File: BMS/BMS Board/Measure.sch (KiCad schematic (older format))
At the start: 53 parts, among them U1 INA149AID, U10 INA149AID, U11 INA149AID, U12 INA149AID, U13 INA149AID, U14 INA149AID, U15 INA149AID, U16 INA149AID, U17 INA149AID, U18 INA149AID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

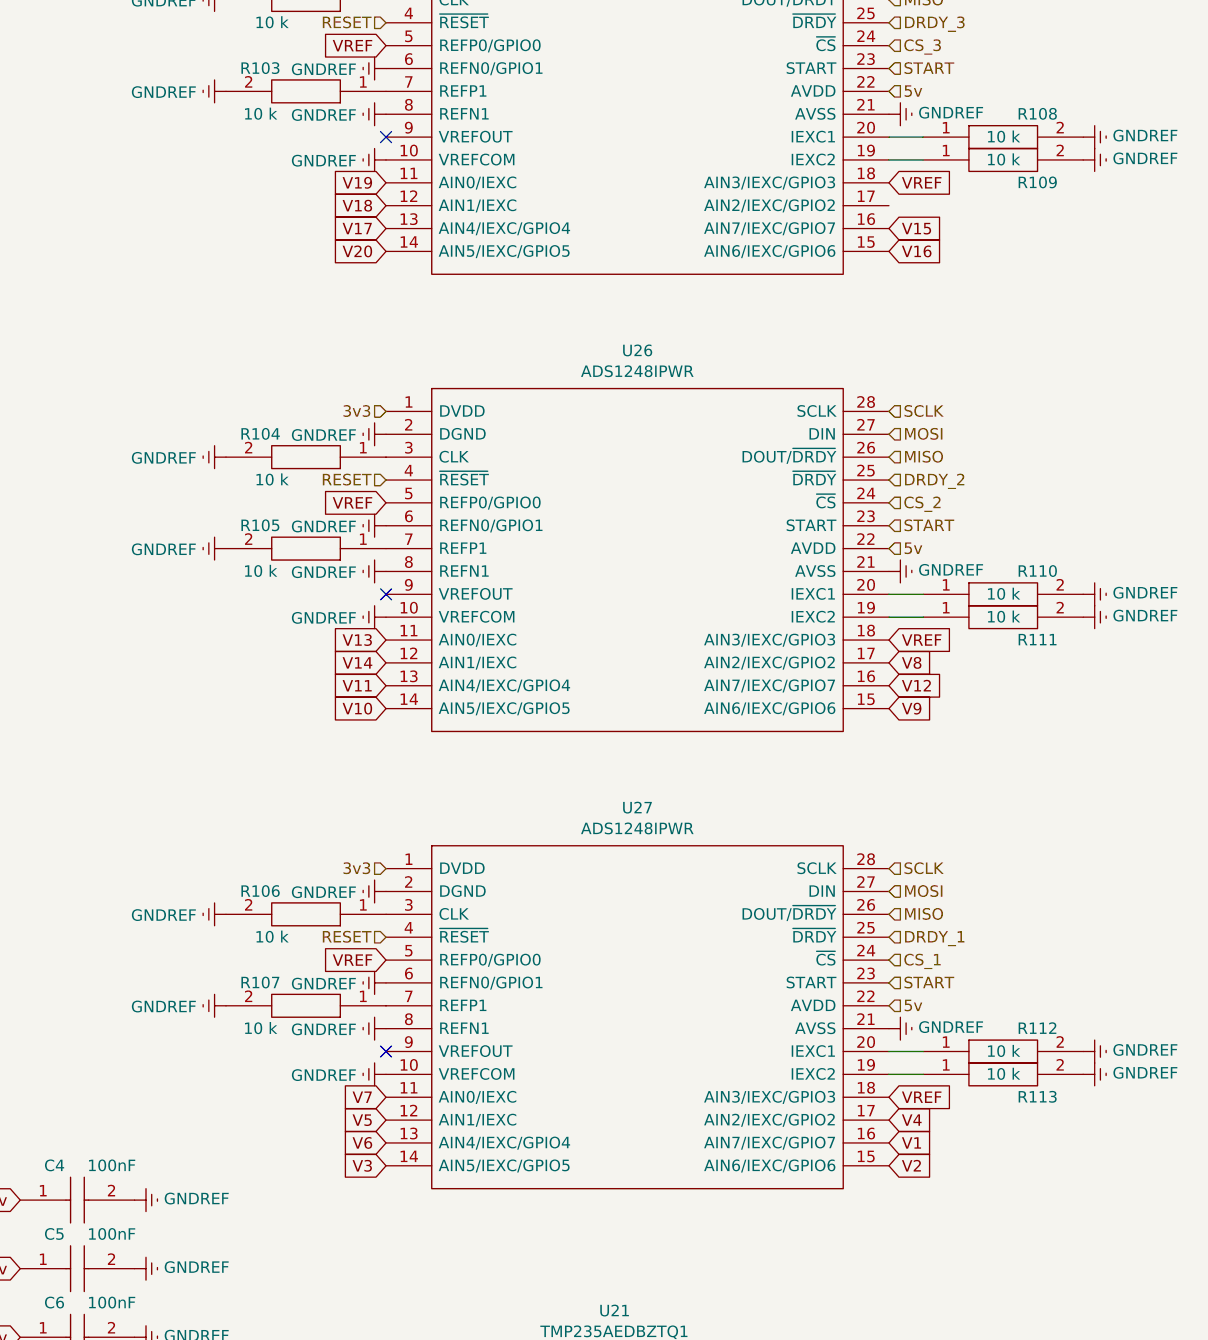
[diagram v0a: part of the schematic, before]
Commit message: changed ui components to be classes instead of methods in Screen class
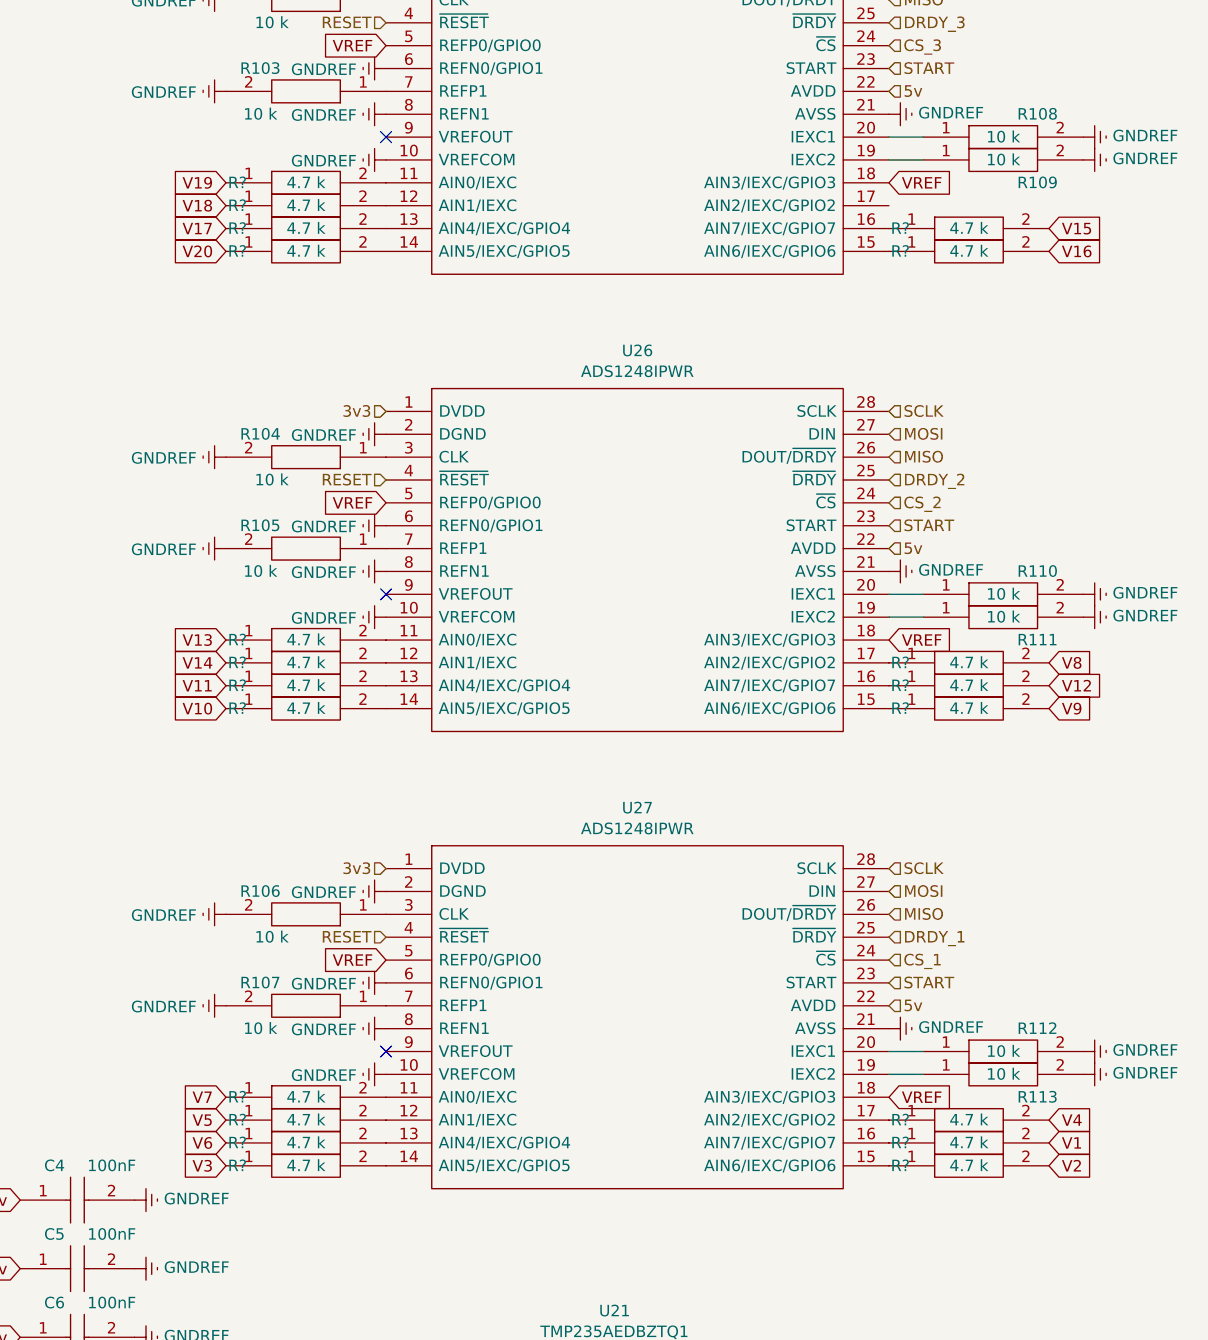
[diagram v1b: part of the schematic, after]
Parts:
- added R? (x20): ERJ-S06J472V, RESC2012X70N, symbol SamacSys_Parts:ERJ-S06J472V
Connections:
- net V1: now also R?.2; no longer U27.16 (AIN7/IEXC/GPIO7)
- net V10: now also R?.1; no longer U26.14 (AIN5/IEXC/GPIO5)
- net V11: now also R?.1; no longer U26.13 (AIN4/IEXC/GPIO4)
- net V12: now also R?.2; no longer U26.16 (AIN7/IEXC/GPIO7)
- net V13: now also R?.1; no longer U26.11 (AIN0/IEXC)
- net V14: now also R?.1; no longer U26.12 (AIN1/IEXC)
- net V15: now also R?.2; no longer U25.16 (AIN7/IEXC/GPIO7)
- net V16: now also R?.2; no longer U25.15 (AIN6/IEXC/GPIO6)
- net V17: now also R?.1; no longer U25.13 (AIN4/IEXC/GPIO4)
- net V18: now also R?.1; no longer U25.12 (AIN1/IEXC)
- net V19: now also R?.1; no longer U25.11 (AIN0/IEXC)
- net V2: now also R?.2; no longer U27.15 (AIN6/IEXC/GPIO6)
- net V20: now also R?.1; no longer U25.14 (AIN5/IEXC/GPIO5)
- net V3: now also R?.1; no longer U27.14 (AIN5/IEXC/GPIO5)
- net V4: now also R?.2; no longer U27.17 (AIN2/IEXC/GPIO2)
- net V5: now also R?.1; no longer U27.12 (AIN1/IEXC)
- net V6: now also R?.1; no longer U27.13 (AIN4/IEXC/GPIO4)
- net V7: now also R?.1; no longer U27.11 (AIN0/IEXC)
- net V8: now also R?.2; no longer U26.17 (AIN2/IEXC/GPIO2)
- net V9: now also R?.2; no longer U26.15 (AIN6/IEXC/GPIO6)
- new net: R?.2, U25.11 (AIN0/IEXC)
- new net: R?.2, U25.12 (AIN1/IEXC)
- new net: R?.2, U25.13 (AIN4/IEXC/GPIO4)
- new net: R?.2, U25.14 (AIN5/IEXC/GPIO5)
- new net: R?.1, U25.15 (AIN6/IEXC/GPIO6)
- new net: R?.1, U25.16 (AIN7/IEXC/GPIO7)
- new net: R?.2, U26.11 (AIN0/IEXC)
- new net: R?.2, U26.12 (AIN1/IEXC)
- new net: R?.2, U26.13 (AIN4/IEXC/GPIO4)
- new net: R?.2, U26.14 (AIN5/IEXC/GPIO5)
- new net: R?.1, U26.15 (AIN6/IEXC/GPIO6)
- new net: R?.1, U26.16 (AIN7/IEXC/GPIO7)
- new net: R?.1, U26.17 (AIN2/IEXC/GPIO2)
- new net: R?.2, U27.11 (AIN0/IEXC)
- new net: R?.2, U27.12 (AIN1/IEXC)
- new net: R?.2, U27.13 (AIN4/IEXC/GPIO4)
- new net: R?.2, U27.14 (AIN5/IEXC/GPIO5)
- new net: R?.1, U27.15 (AIN6/IEXC/GPIO6)
- new net: R?.1, U27.16 (AIN7/IEXC/GPIO7)
- new net: R?.1, U27.17 (AIN2/IEXC/GPIO2)

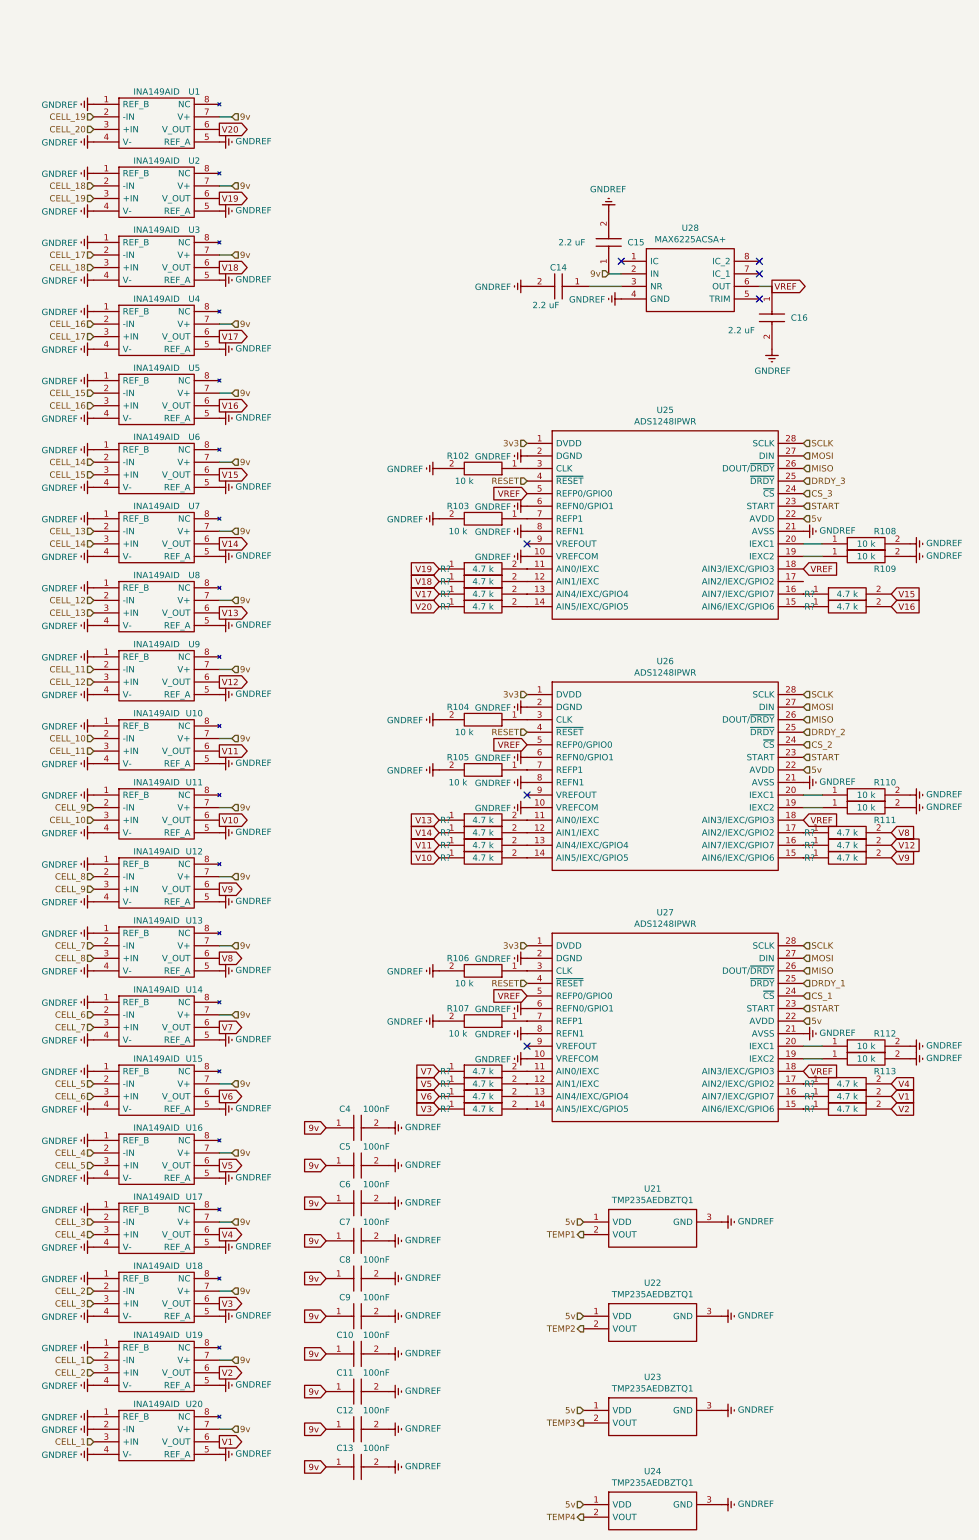
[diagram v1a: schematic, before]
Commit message: "SingleDigitNumberSelector" now blinks when idle.
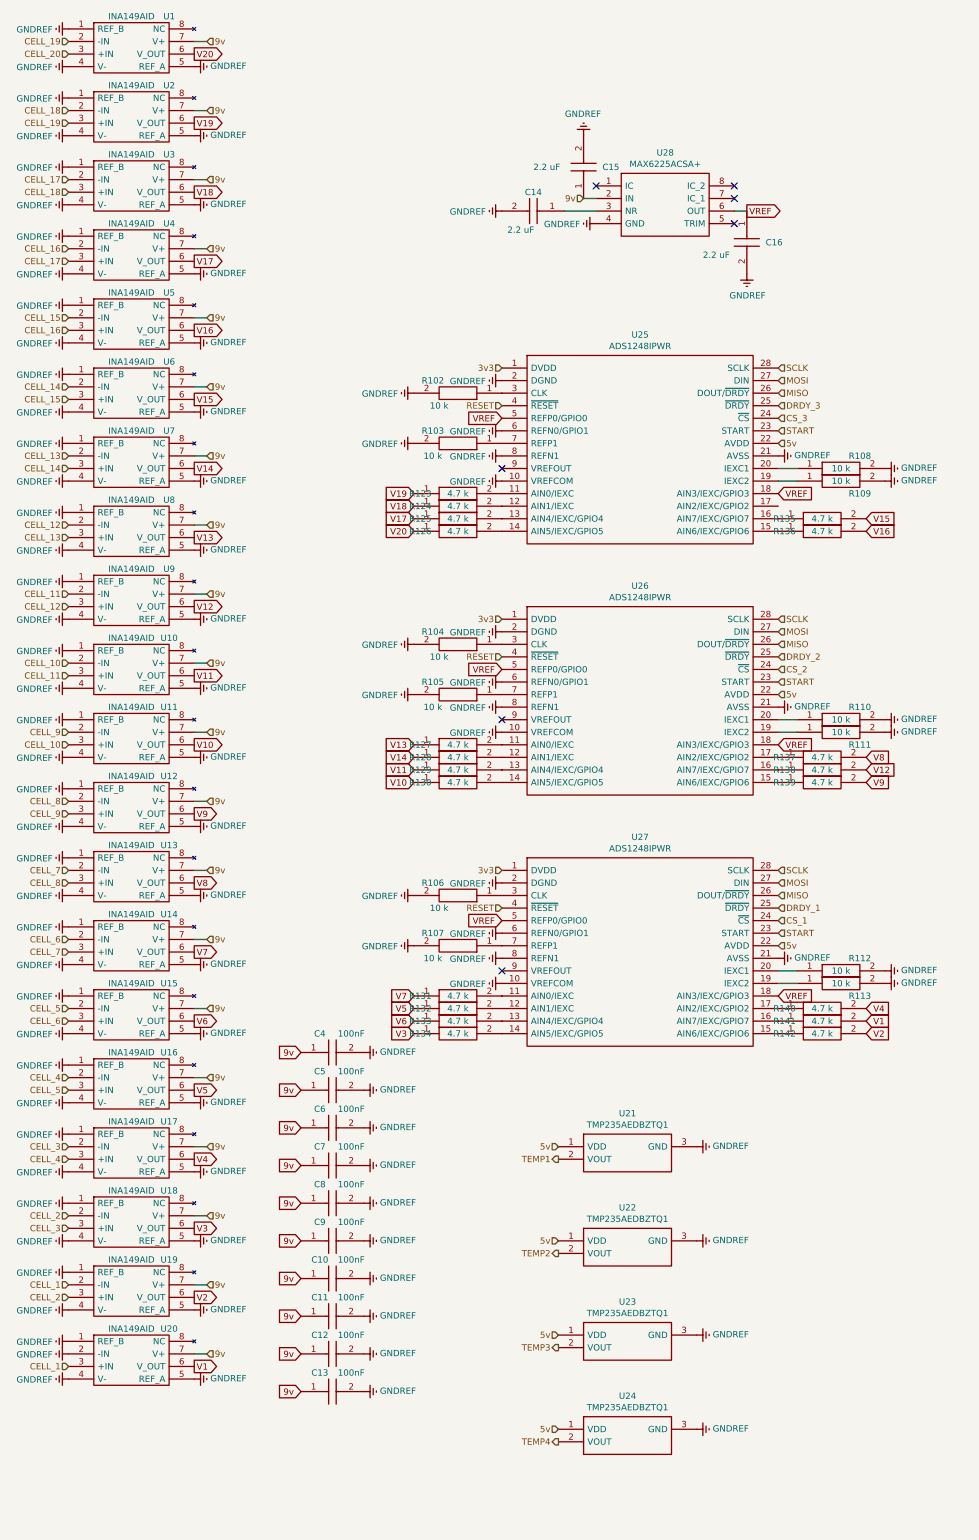
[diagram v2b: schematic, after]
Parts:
- gave numbers to parts that had none: 20
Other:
- moved on the sheet: C10, C11, C12, C13, C14, C15, C16, C4, C5, C6, C7, C8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
